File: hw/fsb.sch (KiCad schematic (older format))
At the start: 15 parts, among them J101 AMPSEAL_8_POS_VERT_WHITE_SEAL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, J102 AMPSEAL_23_POS_VERT_WHITE_SEA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

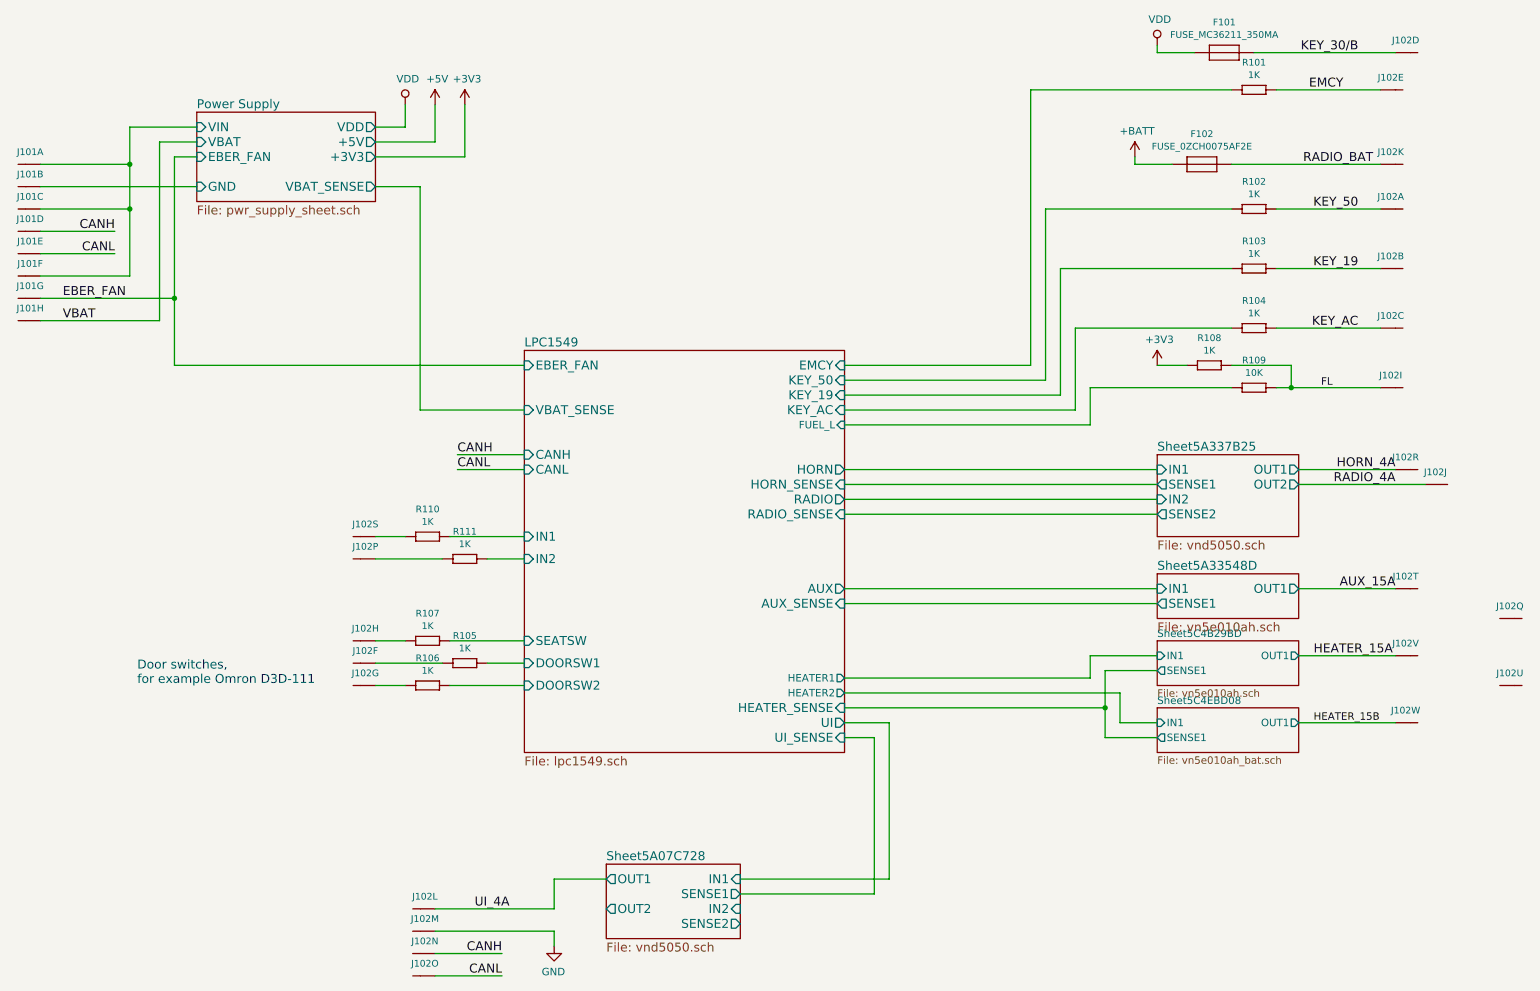
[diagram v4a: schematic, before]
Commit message: coolvalve added to fsb
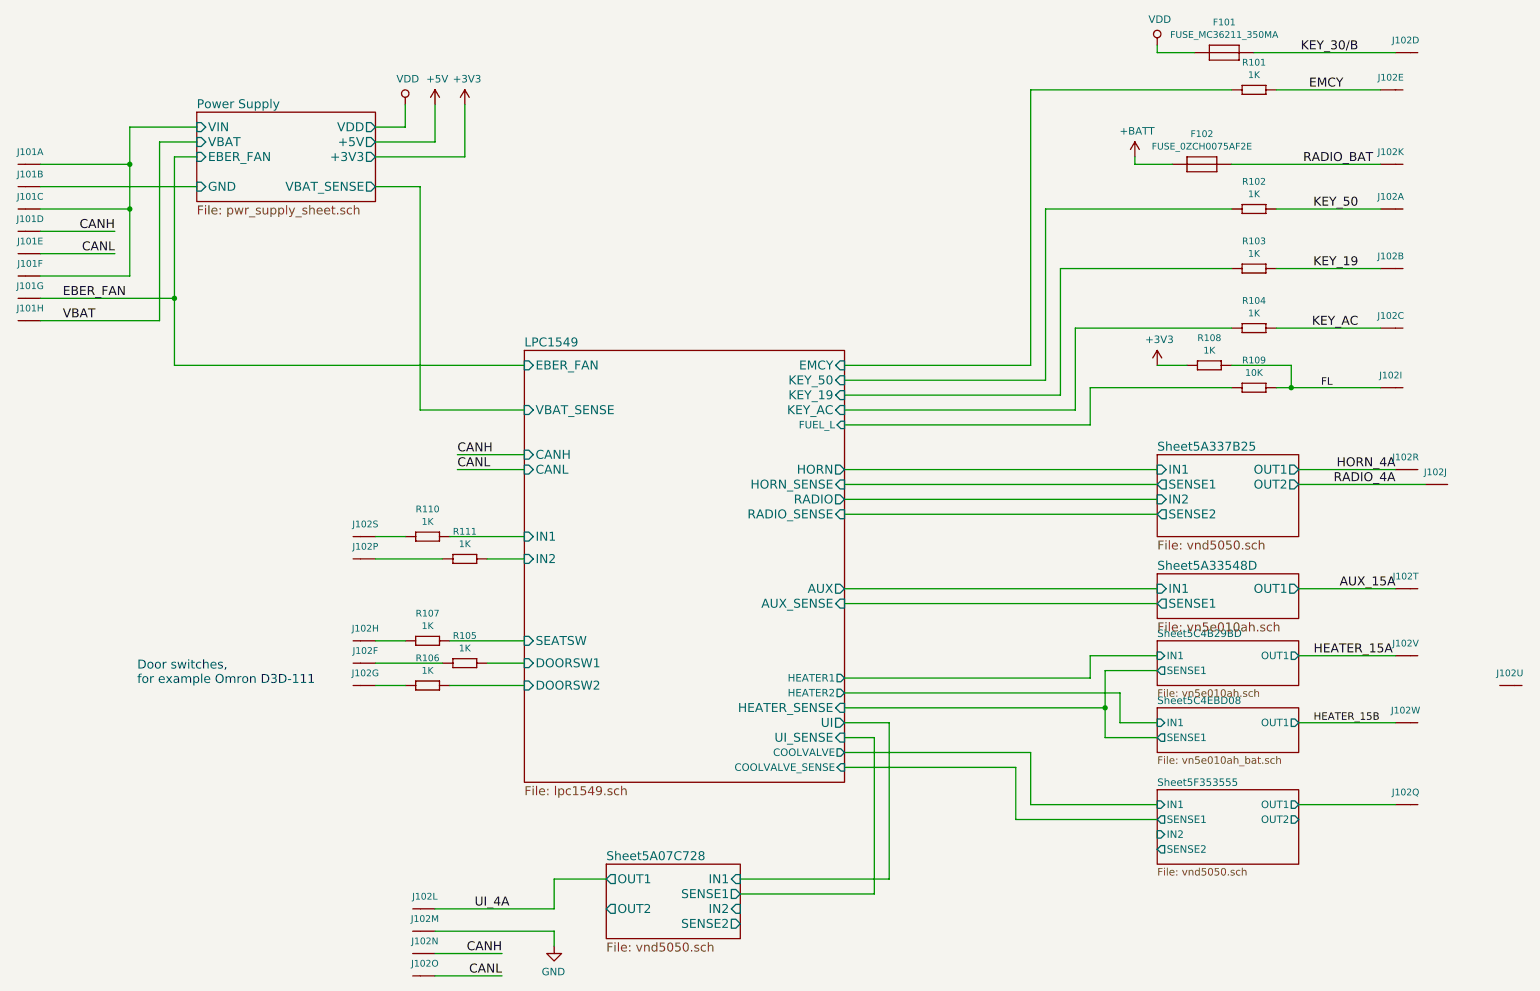
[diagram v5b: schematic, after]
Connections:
- net Sheet5F353555/OUT1: now reaches J102.P$17 (S)
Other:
- moved on the sheet: J102Q
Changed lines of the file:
@@
 $Descr A4 11693 8268
 encoding utf-8
-Sheet 1 8
+Sheet 1 9
 Title "Usewood Ceiling Supply Board"
 Date "2017-06-28"
@@
 CANL
 $Sheet
-S 4250 2800 2150 2700
+S 4250 2800 2150 2900
 U 5953E91C
 F0 "LPC1549" 60
@@
 F25 "HEATER1" O R 6400 5000 50
 F26 "HEATER2" O R 6400 5100 50
+F27 "COOLVALVE" O R 6400 5500 50
+F28 "COOLVALVE_SENSE" I R 6400 5600 50
 $EndSheet
 $Comp
@@
 L fsb-rescue:AMPSEAL_23_POS_VERT_WHITE_SEALED_1-776228-2-RESCUE-fsb J102
 U 17 1 5988B846
-P 10900 4600
-F 0 "J102" H 10868 4683 45  0000 C CNN
-F 1 "AMPSEAL_23_POS_VERT_WHITE_SEALED_1-776228-2" H 10900 4600 45  0001 L BNN
-F 2 "usevolt:AMPSEAL_23_POS_776200-1" H 10930 4750 20  0001 C CNN
-F 3 "http://www.mouser.com/ds/2/418/NG_CD_776228_C13-692101.pdf" H 11000 4570 60  0001 C CNN
-F 4 "571-1-776228-2" H 11400 4970 60  0001 C CNN "1st Source Part Number"
-F 5 "1-776228-2" H 11200 4770 60  0001 C CNN "Manufacturer Part Number"
-F 6 "Mouser" H 11300 4870 60  0001 C CNN "1st Source"
-F 7 "TE Connectivity" H 11100 4670 60  0001 C CNN "Manufacturer"
-	17   10900 4600
+P 10200 5850
+F 0 "J102" H 10168 5933 45  0000 C CNN
+F 1 "AMPSEAL_23_POS_VERT_WHITE_SEALED_1-776228-2" H 10200 5850 45  0001 L BNN
+F 2 "usevolt:AMPSEAL_23_POS_776200-1" H 10230 6000 20  0001 C CNN
+F 3 "http://www.mouser.com/ds/2/418/NG_CD_776228_C13-692101.pdf" H 10300 5820 60  0001 C CNN
+F 4 "571-1-776228-2" H 10700 6220 60  0001 C CNN "1st Source Part Number"
+F 5 "1-776228-2" H 10500 6020 60  0001 C CNN "Manufacturer Part Number"
+F 6 "Mouser" H 10600 6120 60  0001 C CNN "1st Source"
+F 7 "TE Connectivity" H 10400 5920 60  0001 C CNN "Manufacturer"
+	17   10200 5850
 	1    0    0    -1
 $EndComp
@@
 F4 "SENSE1" O L 8500 5400 50
 $EndSheet
+$Sheet
+S 8500 5750 950  500
+U 5F353556
+F0 "Sheet5F353555" 50
+F1 "vnd5050.sch" 50
+F2 "OUT1" O R 9450 5850 50
+F3 "OUT2" O R 9450 5950 50
+F4 "IN1" I L 8500 5850 50
+F5 "IN2" I L 8500 6050 50
+F6 "SENSE1" O L 8500 5950 50
+F7 "SENSE2" O L 8500 6150 50
+$EndSheet
+Wire Wire Line
+	10100 5850 9450 5850
+Wire Wire Line
+	6400 5500 7650 5500
+Wire Wire Line
+	7650 5500 7650 5850
+Wire Wire Line
+	7650 5850 8500 5850
+Wire Wire Line
+	8500 5950 7550 5950
+Wire Wire Line
+	7550 5950 7550 5600
+Wire Wire Line
+	7550 5600 6400 5600
 $EndSCHEMATC
